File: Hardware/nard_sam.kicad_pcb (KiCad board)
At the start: 4 copper layers, 63.5 x 21 mm, 27 parts, among them J1 SIM_Card, J2 SIM_Card, J3 Conn_01x08, J4 Conn_01x10, J6 M20-7910842R, J7 M20-7911042R, U1 SEC1210

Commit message: update project to kicad 8.0
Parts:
- renumbered locked to J5

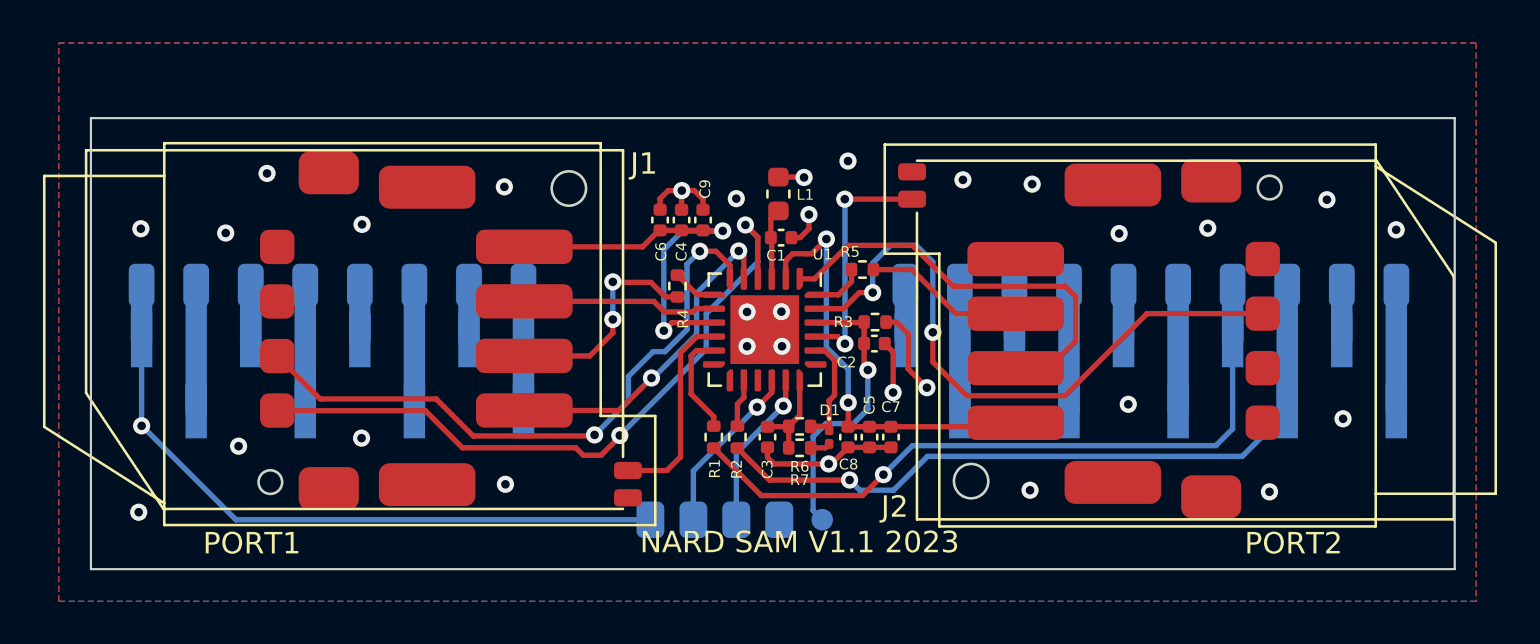
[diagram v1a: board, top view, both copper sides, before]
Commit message: added footprint for placing a eSIM chip directly on the PCB
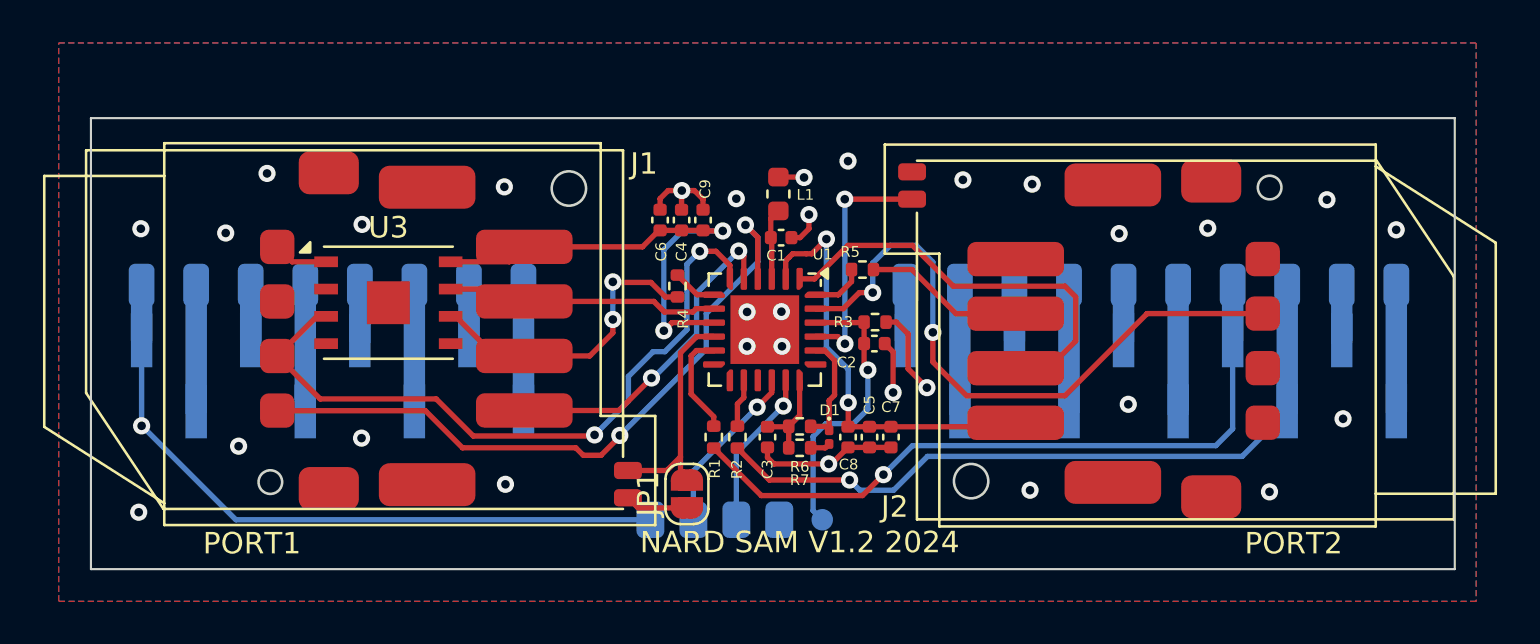
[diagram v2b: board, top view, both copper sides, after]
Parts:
- added JP1: hardwire detect, Jumper:SolderJumper-2_P1.3mm_Open_RoundedPad1.0x1.5mm, F.Cu at (99.5, 77.5)
- added U3: ST4SIM-200M, nard_sam:ST4SIM-200M, F.Cu at (85.6, 68.6)
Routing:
- net GND: track 29.3 -> 34.8 mm
- net /SC1_CLK: track 10.2 -> 14.4 mm
- net /SC1_VCC: track 18.9 -> 22.7 mm
- net /SC1_RST: track 9.10 -> 12.8 mm
- net /SC1_IO: track 29.5 -> 32.6 mm
- net /SC1_PRSNT: track 9.43 -> 10.6 mm
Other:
- board text added: "NARD SAM V1.2 2024"
- board text removed: "NARD SAM V1.1 2023"
